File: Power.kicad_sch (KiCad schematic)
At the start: 45 parts, among them J6 Screw_Terminal_01x03, T1 230/6, T2 78250MC-R, U3 LF50_TO252, U4 LD3985G33R_TSOT23, U5 SN6507DGQ, U6 LD3985G33R_TSOT23

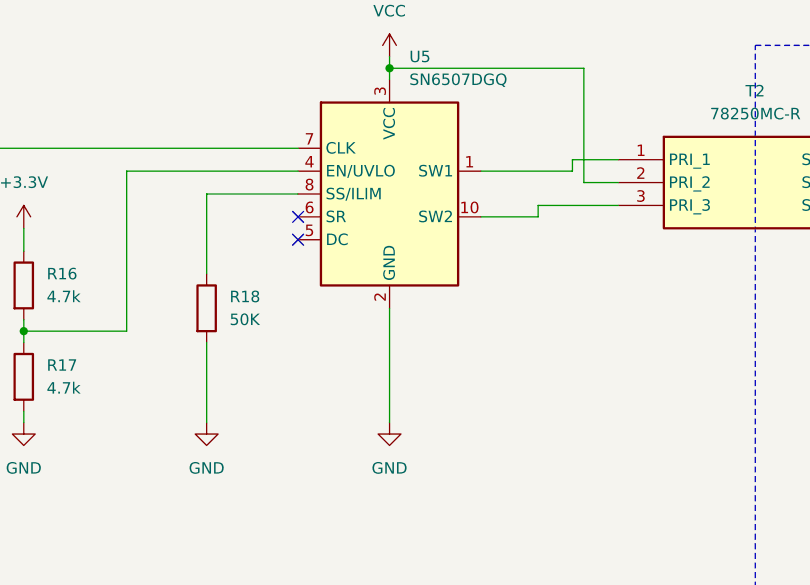
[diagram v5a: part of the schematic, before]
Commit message: Fixes on schematics and footprint update
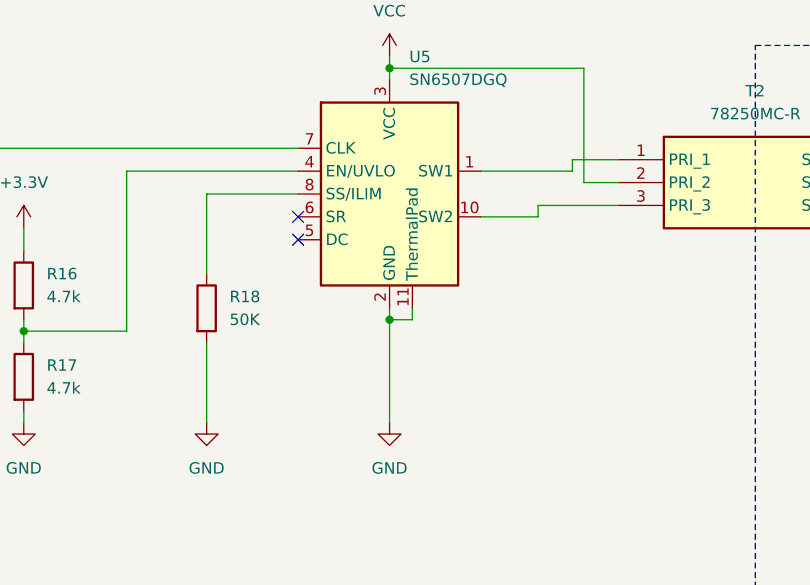
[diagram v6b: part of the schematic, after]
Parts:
- C10, C11, C13, C15, C18, C19, C21, C22, C23, C24: footprint Capacitor_SMD:C_0603_1608Metric_Pad1.08x0.95mm_HandSolder -> Capacitor_SMD:C_0805_2012Metric_Pad1.18x1.45mm_HandSolder
- R12, R13, R14, R16, R17, R18, R20, R21: footprint Resistor_SMD:R_0603_1608Metric_Pad0.98x0.95mm_HandSolder -> Resistor_SMD:R_0805_2012Metric_Pad1.20x1.40mm_HandSolder
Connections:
- net GND: now also U5.11 (ThermalPad)
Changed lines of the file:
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@@
 (kicad_sch (version 20230121) (generator eeschema)
   (paper "A4")
+  (junction (at 151.13 99.06) (diameter 0) (color 0 0 0 0)
+  )
   (junction (at 80.01 48.26) (diameter 0) (color 0 0 0 0)
   )
@@
     (stroke (width 0) (type default))
   )
+  (wire (pts (xy 151.13 99.06) (xy 151.13 110.49))
+    (stroke (width 0) (type default))
+  )
   (wire (pts (xy 64.77 110.49) (xy 64.77 115.57))
     (stroke (width 0) (type default))
@@
     (stroke (width 0) (type default))
   )
+  (wire (pts (xy 153.67 97.79) (xy 153.67 99.06))
+    (stroke (width 0) (type default))
+  )
   (wire (pts (xy 151.13 48.26) (xy 184.15 48.26))
     (stroke (width 0) (type default))
@@
     (stroke (width 0) (type default))
   )
-  (wire (pts (xy 151.13 97.79) (xy 151.13 110.49))
+  (wire (pts (xy 151.13 97.79) (xy 151.13 99.06))
     (stroke (width 0) (type default))
   )
@@
   )
   (wire (pts (xy 125.73 27.94) (xy 151.13 27.94))
+    (stroke (width 0) (type default))
+  )
+  (wire (pts (xy 153.67 99.06) (xy 151.13 99.06))
     (stroke (width 0) (type default))
   )
@@
       (effects (font (size 1.27 1.27)) (justify left))
     )
-    (property "Footprint" "Resistor_SMD:R_0603_1608Metric_Pad0.98x0.95mm_HandSolder" (at 96.012 97.79 90)
+    (property "Footprint" "Resistor_SMD:R_0805_2012Metric_Pad1.20x1.40mm_HandSolder" (at 96.012 97.79 90)
       (effects (font (size 1.27 1.27)) hide)
     )
@@
       (effects (font (size 1.27 1.27)) (justify left))
     )
-    (property "Footprint" "Resistor_SMD:R_0603_1608Metric_Pad0.98x0.95mm_HandSolder" (at 74.422 72.39 90)
+    (property "Footprint" "Resistor_SMD:R_0805_2012Metric_Pad1.20x1.40mm_HandSolder" (at 74.422 72.39 90)
       (effects (font (size 1.27 1.27)) hide)
     )
@@
       (effects (font (size 1.27 1.27)) (justify left))
     )
-    (property "Footprint" "Capacitor_SMD:C_0603_1608Metric_Pad1.08x0.95mm_HandSolder" (at 252.4252 95.25 0)
+    (property "Footprint" "Capacitor_SMD:C_0805_2012Metric_Pad1.18x1.45mm_HandSolder" (at 252.4252 95.25 0)
       (effects (font (size 1.27 1.27)) hide)
     )
@@
       (effects (font (size 1.27 1.27)) (justify left))
     )
-    (property "Footprint" "Resistor_SMD:R_0603_1608Metric_Pad0.98x0.95mm_HandSolder" (at 108.712 95.25 90)
+    (property "Footprint" "Resistor_SMD:R_0805_2012Metric_Pad1.20x1.40mm_HandSolder" (at 108.712 95.25 90)
       (effects (font (size 1.27 1.27)) hide)
     )
@@
       (effects (font (size 1.27 1.27)) (justify left))
     )
-    (property "Footprint" "Capacitor_SMD:C_0603_1608Metric_Pad1.08x0.95mm_HandSolder" (at 28.9052 121.92 0)
+    (property "Footprint" "Capacitor_SMD:C_0805_2012Metric_Pad1.18x1.45mm_HandSolder" (at 28.9052 121.92 0)
       (effects (font (size 1.27 1.27)) hide)
     )
@@
       (effects (font (size 1.27 1.27)) (justify left))
     )
-    (property "Footprint" "Capacitor_SMD:C_0603_1608Metric_Pad1.08x0.95mm_HandSolder" (at 65.7352 123.19 0)
+    (property "Footprint" "Capacitor_SMD:C_0805_2012Metric_Pad1.18x1.45mm_HandSolder" (at 65.7352 123.19 0)
       (effects (font (size 1.27 1.27)) hide)
     )
@@
       (effects (font (size 1.27 1.27)) (justify left))
     )
-    (property "Footprint" "Resistor_SMD:R_0603_1608Metric_Pad0.98x0.95mm_HandSolder" (at 74.422 115.57 90)
+    (property "Footprint" "Resistor_SMD:R_0805_2012Metric_Pad1.20x1.40mm_HandSolder" (at 74.422 115.57 90)
       (effects (font (size 1.27 1.27)) hide)
     )
@@
       (effects (font (size 1.27 1.27)) (justify left))
     )
-    (property "Footprint" "Capacitor_SMD:C_0603_1608Metric_Pad1.08x0.95mm_HandSolder" (at 242.2652 138.43 0)
+    (property "Footprint" "Capacitor_SMD:C_0805_2012Metric_Pad1.18x1.45mm_HandSolder" (at 242.2652 138.43 0)
       (effects (font (size 1.27 1.27)) hide)
     )
@@
       (effects (font (size 1.27 1.27)) (justify left))
     )
-    (property "Footprint" "Resistor_SMD:R_0603_1608Metric_Pad0.98x0.95mm_HandSolder" (at 108.712 105.41 90)
+    (property "Footprint" "Resistor_SMD:R_0805_2012Metric_Pad1.20x1.40mm_HandSolder" (at 108.712 105.41 90)
       (effects (font (size 1.27 1.27)) hide)
     )
@@
       (effects (font (size 1.27 1.27)) (justify left))
     )
-    (property "Footprint" "Resistor_SMD:R_0603_1608Metric_Pad0.98x0.95mm_HandSolder" (at 259.842 91.44 90)
+    (property "Footprint" "Resistor_SMD:R_0805_2012Metric_Pad1.20x1.40mm_HandSolder" (at 259.842 91.44 90)
       (effects (font (size 1.27 1.27)) hide)
     )
@@
       (effects (font (size 1.27 1.27)) (justify left))
     )
-    (property "Footprint" "Resistor_SMD:R_0603_1608Metric_Pad0.98x0.95mm_HandSolder" (at 262.382 130.81 90)
+    (property "Footprint" "Resistor_SMD:R_0805_2012Metric_Pad1.20x1.40mm_HandSolder" (at 262.382 130.81 90)
       (effects (font (size 1.27 1.27)) hide)
     )
@@
       (effects (font (size 1.27 1.27)) (justify left))
     )
-    (property "Footprint" "Capacitor_SMD:C_0603_1608Metric_Pad1.08x0.95mm_HandSolder" (at 152.0952 46.99 0)
+    (property "Footprint" "Capacitor_SMD:C_0805_2012Metric_Pad1.18x1.45mm_HandSolder" (at 152.0952 46.99 0)
       (effects (font (size 1.27 1.27)) hide)
     )
@@
       (effects (font (size 1.27 1.27)) (justify left))
     )
-    (property "Footprint" "Capacitor_SMD:C_0603_1608Metric_Pad1.08x0.95mm_HandSolder" (at 242.2652 95.25 0)
+    (property "Footprint" "Capacitor_SMD:C_0805_2012Metric_Pad1.18x1.45mm_HandSolder" (at 242.2652 95.25 0)
       (effects (font (size 1.27 1.27)) hide)
     )
@@
       (effects (font (size 1.27 1.27)) (justify left))
     )
-    (property "Footprint" "Capacitor_SMD:C_0603_1608Metric_Pad1.08x0.95mm_HandSolder" (at 54.3052 123.19 0)
+    (property "Footprint" "Capacitor_SMD:C_0805_2012Metric_Pad1.18x1.45mm_HandSolder" (at 54.3052 123.19 0)
       (effects (font (size 1.27 1.27)) hide)
     )
@@
     (pin "3")
     (pin "7")
+    (pin "11")
     (instances
       (project "Eng_Thesis"
@@
       (effects (font (size 1.27 1.27)) (justify left))
     )
-    (property "Footprint" "Resistor_SMD:R_0603_1608Metric_Pad0.98x0.95mm_HandSolder" (at 129.032 97.79 90)
+    (property "Footprint" "Resistor_SMD:R_0805_2012Metric_Pad1.20x1.40mm_HandSolder" (at 129.032 97.79 90)
       (effects (font (size 1.27 1.27)) hide)
     )
@@
       (effects (font (size 1.27 1.27)) (justify left))
     )
-    (property "Footprint" "Capacitor_SMD:C_0603_1608Metric_Pad1.08x0.95mm_HandSolder" (at 253.6952 138.43 0)
+    (property "Footprint" "Capacitor_SMD:C_0805_2012Metric_Pad1.18x1.45mm_HandSolder" (at 253.6952 138.43 0)
       (effects (font (size 1.27 1.27)) hide)
     )
@@
       (effects (font (size 1.27 1.27)) (justify left))
     )
-    (property "Footprint" "Capacitor_SMD:C_0603_1608Metric_Pad1.08x0.95mm_HandSolder" (at 216.8652 137.16 0)
+    (property "Footprint" "Capacitor_SMD:C_0805_2012Metric_Pad1.18x1.45mm_HandSolder" (at 216.8652 137.16 0)
       (effects (font (size 1.27 1.27)) hide)
     )
@@
       (effects (font (size 1.27 1.27)) (justify left))
     )
-    (property "Footprint" "Capacitor_SMD:C_0603_1608Metric_Pad1.08x0.95mm_HandSolder" (at 33.9852 80.01 0)
-      (effects (font (size 1.27 1.27)) hide)
-    )
+    (property "Footprint" "Capacitor_SMD:C_0805_2012Metric_Pad1.18x1.45mm_HandSolder" (at 33.9852 80.01 0)
+      (effects (font (size 1.27 1.27)) hide)
+    )

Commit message: v.0.1
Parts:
- removed C14: 100n, Capacitor_THT:C_Rect_L18.0mm_W6.0mm_P15.00mm_FKS3_FKP3, symbol Device:C
- removed C16, C17: 2,2n, Capacitor_THT:C_Disc_D10.5mm_W5.0mm_P7.50mm, symbol Device:C
- removed C18: 100u, Capacitor_SMD:C_0805_2012Metric_Pad1.18x1.45mm_HandSolder, symbol Device:C
- removed C20: 6800u, Capacitor_THT:CP_Radial_D18.0mm_P7.50mm, symbol Device:C_Polarized
- removed D3: LED, LED_SMD:LED_0603_1608Metric_Pad1.05x0.95mm_HandSolder, symbol Device:LED
- removed D4: ABS8, Diode_SMD:Diode_Bridge_Diotec_ABS, symbol Diode_Bridge:ABS8
- removed J6: Screw_Terminal_01x03, LibLoader:XY126V-3P, symbol Connector:Screw_Terminal_01x03
- removed R13: 1k, Resistor_SMD:R_0805_2012Metric_Pad1.20x1.40mm_HandSolder, symbol Device:R
- removed R19: 100R, Resistor_SMD:R_2512_6332Metric_Pad1.40x3.35mm_HandSolder, symbol Device:R
- removed T1: 230/6, Transformer_THT:TSZZ4.5003M, symbol Device:Transformer_1P_1S
- removed TP4: 3V3, TestPoint:TestPoint_Pad_1.5x1.5mm, symbol Connector:TestPoint
- removed TP5: BrOut, TestPoint:TestPoint_Pad_1.5x1.5mm, symbol Connector:TestPoint
- added D4: D_Zener, Diode_SMD:D_MELF, symbol Device:D_Zener
- added J6: Jack-DC, LibLoader:PCGK21, symbol Connector:Jack-DC
- added Q1: Q_PMOS_GSD, Package_TO_SOT_SMD:SOT-23_Handsoldering, symbol Device:Q_PMOS_GSD
- F1: value 315mA -> Fuse
- R11: value 1M -> 1k; footprint Resistor_SMD:R_1206_3216Metric_Pad1.30x1.75mm_HandSolder -> Resistor_SMD:R_0805_2012Metric_Pad1.20x1.40mm_HandSolder
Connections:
- net GND: now also R11.2, J6.2
- net VCC: now also D4.1 (K), Q1.2 (S)
- net at R11.1: now also D4.2 (A), Q1.1 (G); no longer F1.2
- net at F1.1: now also J6.1
- new net: F1.2, Q1.3 (D)
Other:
- moved on the sheet: C10, C11, C12, C13, C15, C19, C21, C22, C23, C24, D2, D5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
